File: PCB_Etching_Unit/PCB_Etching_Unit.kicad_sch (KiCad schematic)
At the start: 89 parts, among them M1 Motor_DC, M2 Motor_DC, Q1 TIP42, Q10 TIP42, Q11 TIP41, Q12 2N3904, Q13 TIP42, Q14 BC550, Q15 BC550, Q16 BC550, Q17 BC550, Q18 BC550, Q19 BC550, Q2 TIP42, Q20 BC550, Q3 TIP42, Q4 TIP42, Q5 TIP42, Q6 TIP41, Q7 TIP41, Q8 TIP42, Q9 TIP41, SW1 SW_MEC_5G, SW2 SW_MEC_5G, SW3 SW_MEC_5G, SW4 SW_MEC_5G, SW5 SW_MEC_5G, SW6 SW_MEC_5G, SW7 SW_MEC_5G, U1 HDSP-7801, U11 4511, U2 HDSP-7801, U3 HDSP-7801, U4 HDSP-7801, U5 4027, U6 4027, U9 4011

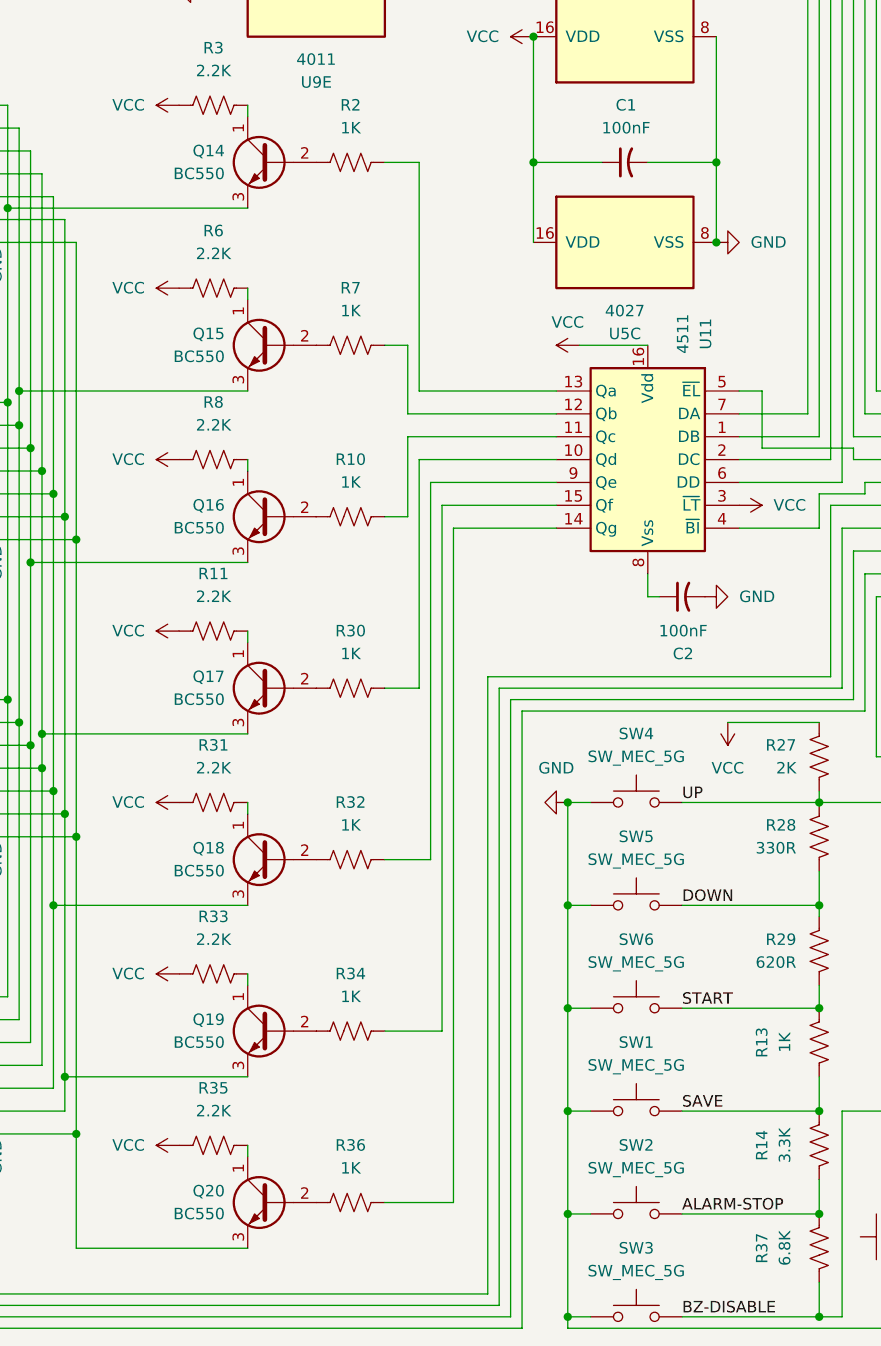
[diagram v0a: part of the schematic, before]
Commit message: 4511 pulls output low to activate, replaced NPN with PNP transistors to do that
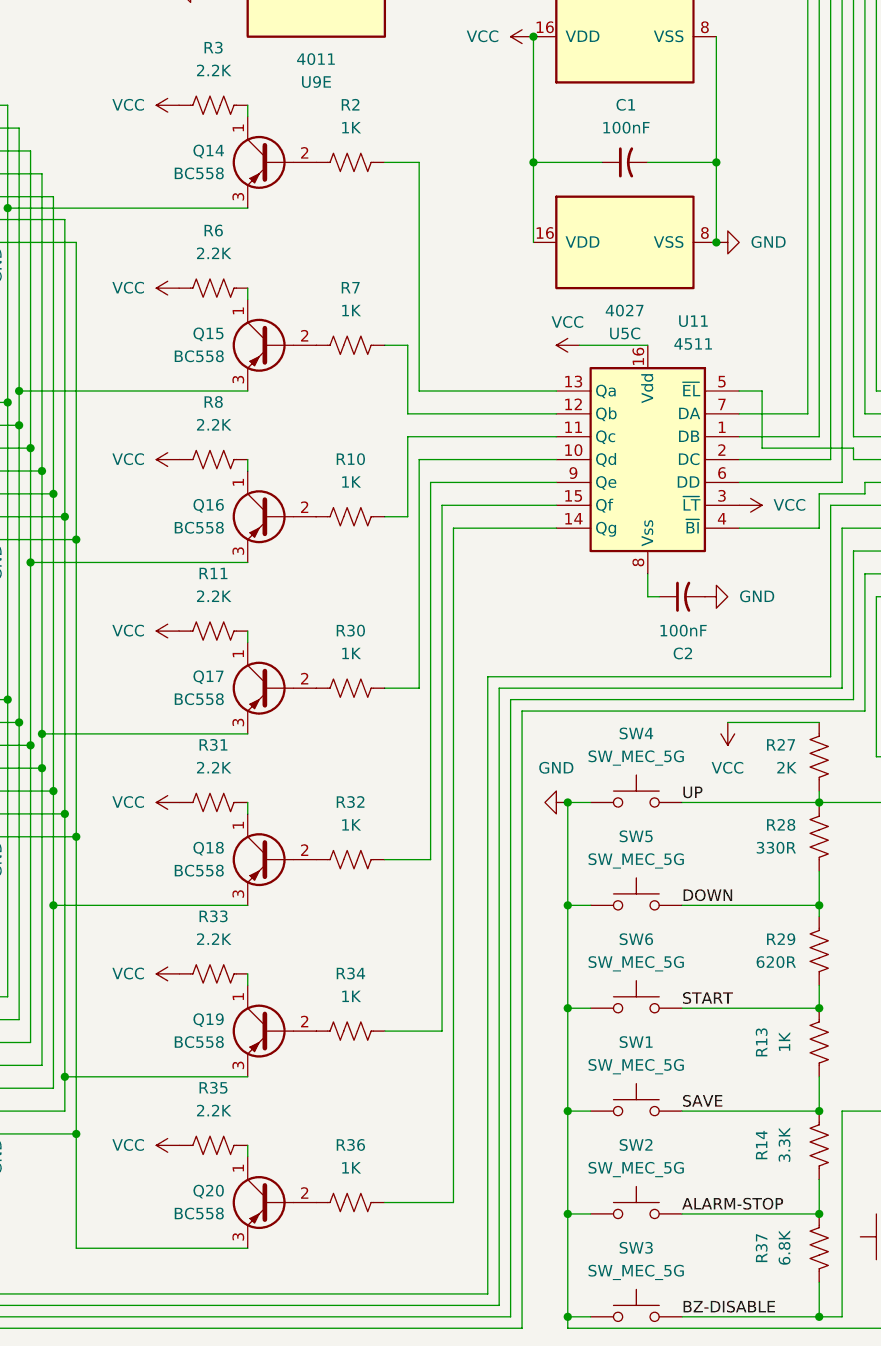
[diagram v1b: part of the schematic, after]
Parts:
- removed Q14, Q15, Q16, Q17, Q18, Q19, Q20: BC550, Package_TO_SOT_THT:TO-92_Inline, symbol Transistor_BJT:BC550
- added Q14, Q15, Q16, Q17, Q18, Q19, Q20: BC558, Package_TO_SOT_THT:TO-92_Inline, symbol Transistor_BJT:BC558
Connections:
- net at R6.2: now also Q15.1 (C)
- net at R31.2: now also Q18.1 (C)
- net at R32.1: now also Q18.2 (B)
- net at U1.4 (E), U2.4 (E), U3.4 (E)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: now also Q18.3 (E)
- net at R36.1: now also Q20.2 (B)
- net at R30.1: now also Q17.2 (B)
- net at R3.1: now also Q14.1 (C)
- net at R2.1: now also Q14.2 (B)
- net at U1.10 (A), U2.10 (A), U3.10 (A)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: now also Q14.3 (E)
- net at R35.2: now also Q20.1 (C)
- net at U1.3 (G), U2.3 (G), U3.3 (G)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: now also Q20.3 (E)
- net at R7.1: now also Q15.2 (B)
- net at U1.9 (B), U2.9 (B), U3.9 (B)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: now also Q15.3 (E)
- net at U1.2 (F), U2.2 (F), U3.2 (F)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: now also Q19.3 (E)
- net at U1.5 (D), U2.5 (D), U3.5 (D)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: now also Q17.3 (E)
- net at U1.8 (C), U2.8 (C), U3.8 (C)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: now also Q16.3 (E)
- net at R8.2: now also Q16.1 (C)
- net at R34.1: now also Q19.2 (B)
- net at R11.2: now also Q17.1 (C)
- net at R33.2: now also Q19.1 (C)
- net at R10.1: now also Q16.2 (B)

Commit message: Updated doc
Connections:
- net at R6.2: now also Q15.3 (E); no longer Q15.1 (C)
- net at Q18.1 (C): now also U1.4 (E), U2.4 (E), U3.4 (E), U4.4 (E); no longer R31.2
- net at Q20.1 (C): now also U1.3 (G), U2.3 (G), U3.3 (G), U4.3 (G); no longer R35.2
- net at U1.10 (A), U2.10 (A), U3.10 (A)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: now also Q14.1 (C); no longer Q14.3 (E)
- net at U1.2 (F), U2.2 (F), U3.2 (F)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: now also Q19.1 (C); no longer Q19.3 (E)
- net at U1.5 (D), U2.5 (D), U3.5 (D)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: now also Q17.1 (C); no longer Q17.3 (E)
- net at U1.8 (C), U2.8 (C), U3.8 (C)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: now also Q16.1 (C); no longer Q16.3 (E)
- net at U1.9 (B), U2.9 (B), U3.9 (B)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: now also Q15.1 (C); no longer Q15.3 (E)
- net at R3.1: now also Q14.3 (E); no longer Q14.1 (C)
- net at R8.2: now also Q16.3 (E); no longer Q16.1 (C)
- net at R11.2: now also Q17.3 (E); no longer Q17.1 (C)
- net at R33.2: now also Q19.3 (E); no longer Q19.1 (C)
- new net: Q18.3 (E), R31.2
- new net: Q20.3 (E), R35.2
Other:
- moved on the sheet: Q14, Q15, Q16, Q17, Q18, Q19, Q20
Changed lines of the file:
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@@
 	(wire
 		(pts
-			(xy 157.48 104.14) (xy 157.48 102.87)
+			(xy 156.21 104.14) (xy 156.21 102.87)
 		)
 		(stroke
@@
 	(wire
 		(pts
-			(xy 157.48 102.87) (xy 163.83 102.87)
+			(xy 156.21 102.87) (xy 163.83 102.87)
 		)
 		(stroke
@@
 	(wire
 		(pts
-			(xy 152.4 104.14) (xy 157.48 104.14)
+			(xy 152.4 104.14) (xy 156.21 104.14)
 		)
 		(stroke
@@
 	(symbol
 		(lib_id "Transistor_BJT:BC558")
-		(at 91.44 144.78 0)
-		(mirror y)
+		(at 91.44 144.78 180)
 		(unit 1)
 		(exclude_from_sim no)
@@
 		(on_board yes)
 		(dnp no)
-		(fields_autoplaced yes)
 		(property "Reference" "Q18"
-			(at 86.36 143.5099 0)
+			(at 86.36 146.0501 0)
 			(effects
 				(font
@@
 		)
 		(property "Value" "BC558"
-			(at 86.36 146.0499 0)
+			(at 86.36 143.5101 0)
 			(effects
 				(font
@@
 		)
 		(property "Footprint" "Package_TO_SOT_THT:TO-92_Inline"
-			(at 86.36 146.685 0)
+			(at 86.36 142.875 0)
 			(effects
 				(font
@@
 	(symbol
 		(lib_id "Transistor_BJT:BC558")
-		(at 91.44 182.88 0)
-		(mirror y)
+		(at 91.44 182.88 180)
 		(unit 1)
 		(exclude_from_sim no)
@@
 		(on_board yes)
 		(dnp no)
-		(fields_autoplaced yes)
 		(property "Reference" "Q20"
-			(at 86.36 181.6099 0)
+			(at 86.36 184.1501 0)
 			(effects
 				(font
@@
 		)
 		(property "Value" "BC558"
-			(at 86.36 184.1499 0)
+			(at 86.36 181.6101 0)
 			(effects
 				(font
@@
 		)
 		(property "Footprint" "Package_TO_SOT_THT:TO-92_Inline"
-			(at 86.36 184.785 0)
+			(at 86.36 180.975 0)
 			(effects
 				(font
@@
 	(symbol
 		(lib_id "Transistor_BJT:BC558")
-		(at 91.44 67.31 0)
-		(mirror y)
+		(at 91.44 67.31 180)
 		(unit 1)
 		(exclude_from_sim no)
@@
 		(on_board yes)
 		(dnp no)
-		(fields_autoplaced yes)
 		(property "Reference" "Q14"
-			(at 86.36 66.0399 0)
+			(at 86.36 68.5801 0)
 			(effects
 				(font
@@
 		)
 		(property "Value" "BC558"
-			(at 86.36 68.5799 0)
+			(at 86.36 66.0401 0)
 			(effects
 				(font
@@
 		)
 		(property "Footprint" "Package_TO_SOT_THT:TO-92_Inline"
-			(at 86.36 69.215 0)
+			(at 86.36 65.405 0)
 			(effects
 				(font
@@
 	(symbol
 		(lib_id "Transistor_BJT:BC558")
-		(at 91.44 87.63 0)
-		(mirror y)
+		(at 91.44 87.63 180)
 		(unit 1)
 		(exclude_from_sim no)
@@
 		(on_board yes)
 		(dnp no)
-		(fields_autoplaced yes)
 		(property "Reference" "Q15"
-			(at 86.36 86.3599 0)
+			(at 86.36 88.9001 0)
 			(effects
 				(font
@@
 		)
 		(property "Value" "BC558"
-			(at 86.36 88.8999 0)
+			(at 86.36 86.3601 0)
 			(effects
 				(font
@@
 		)
 		(property "Footprint" "Package_TO_SOT_THT:TO-92_Inline"
-			(at 86.36 89.535 0)
+			(at 86.36 85.725 0)
 			(effects
 				(font
@@
 	(symbol
 		(lib_id "Transistor_BJT:BC558")
-		(at 91.44 163.83 0)
-		(mirror y)
+		(at 91.44 163.83 180)
 		(unit 1)
 		(exclude_from_sim no)
@@
 		(on_board yes)
 		(dnp no)
-		(fields_autoplaced yes)
 		(property "Reference" "Q19"
-			(at 86.36 162.5599 0)
+			(at 86.36 165.1001 0)
 			(effects
 				(font
@@
 		)
 		(property "Value" "BC558"
-			(at 86.36 165.0999 0)
+			(at 86.36 162.5601 0)
 			(effects
 				(font
@@
 		)
 		(property "Footprint" "Package_TO_SOT_THT:TO-92_Inline"
-			(at 86.36 165.735 0)
+			(at 86.36 161.925 0)
 			(effects
 				(font
@@
 	(symbol
 		(lib_id "Transistor_BJT:BC558")
-		(at 91.44 125.73 0)
-		(mirror y)
+		(at 91.44 125.73 180)
 		(unit 1)
 		(exclude_from_sim no)
@@
 		(on_board yes)
 		(dnp no)
-		(fields_autoplaced yes)
 		(property "Reference" "Q17"
-			(at 86.36 124.4599 0)
+			(at 86.36 127.0001 0)
 			(effects
 				(font
@@
 		)
 		(property "Value" "BC558"
-			(at 86.36 126.9999 0)
+			(at 86.36 124.4601 0)
 			(effects
 				(font
@@
 		)
 		(property "Footprint" "Package_TO_SOT_THT:TO-92_Inline"
-			(at 86.36 127.635 0)
+			(at 86.36 123.825 0)
 			(effects
 				(font
@@
 	(symbol
 		(lib_id "Transistor_BJT:BC558")
-		(at 91.44 106.68 0)
-		(mirror y)
+		(at 91.44 106.68 180)
 		(unit 1)
 		(exclude_from_sim no)
@@
 		(on_board yes)
 		(dnp no)
-		(fields_autoplaced yes)
 		(property "Reference" "Q16"
-			(at 86.36 105.4099 0)
+			(at 86.36 107.9501 0)
 			(effects
 				(font
@@
 		)
 		(property "Value" "BC558"
-			(at 86.36 107.9499 0)
+			(at 86.36 105.4101 0)
 			(effects
 				(font
@@
 		)
 		(property "Footprint" "Package_TO_SOT_THT:TO-92_Inline"
-			(at 86.36 108.585 0)
+			(at 86.36 104.775 0)
 			(effects
 				(font

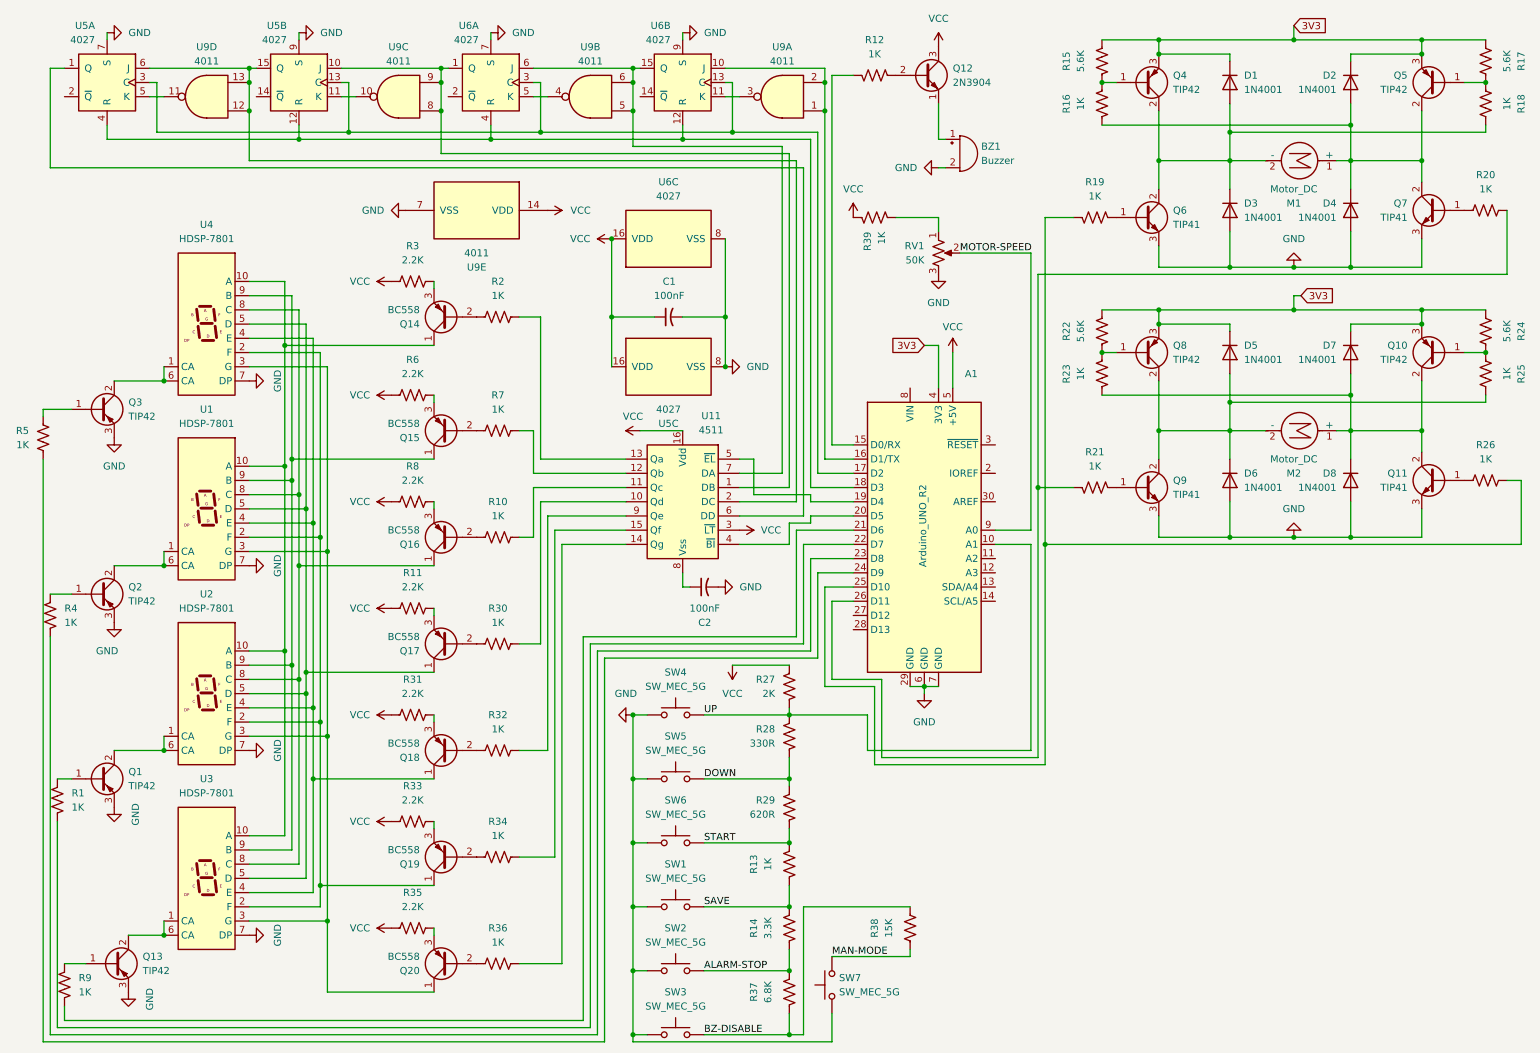
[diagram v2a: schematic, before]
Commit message: Next person to mix up PNP transistors gets bolted. Flipped transistors at segment output
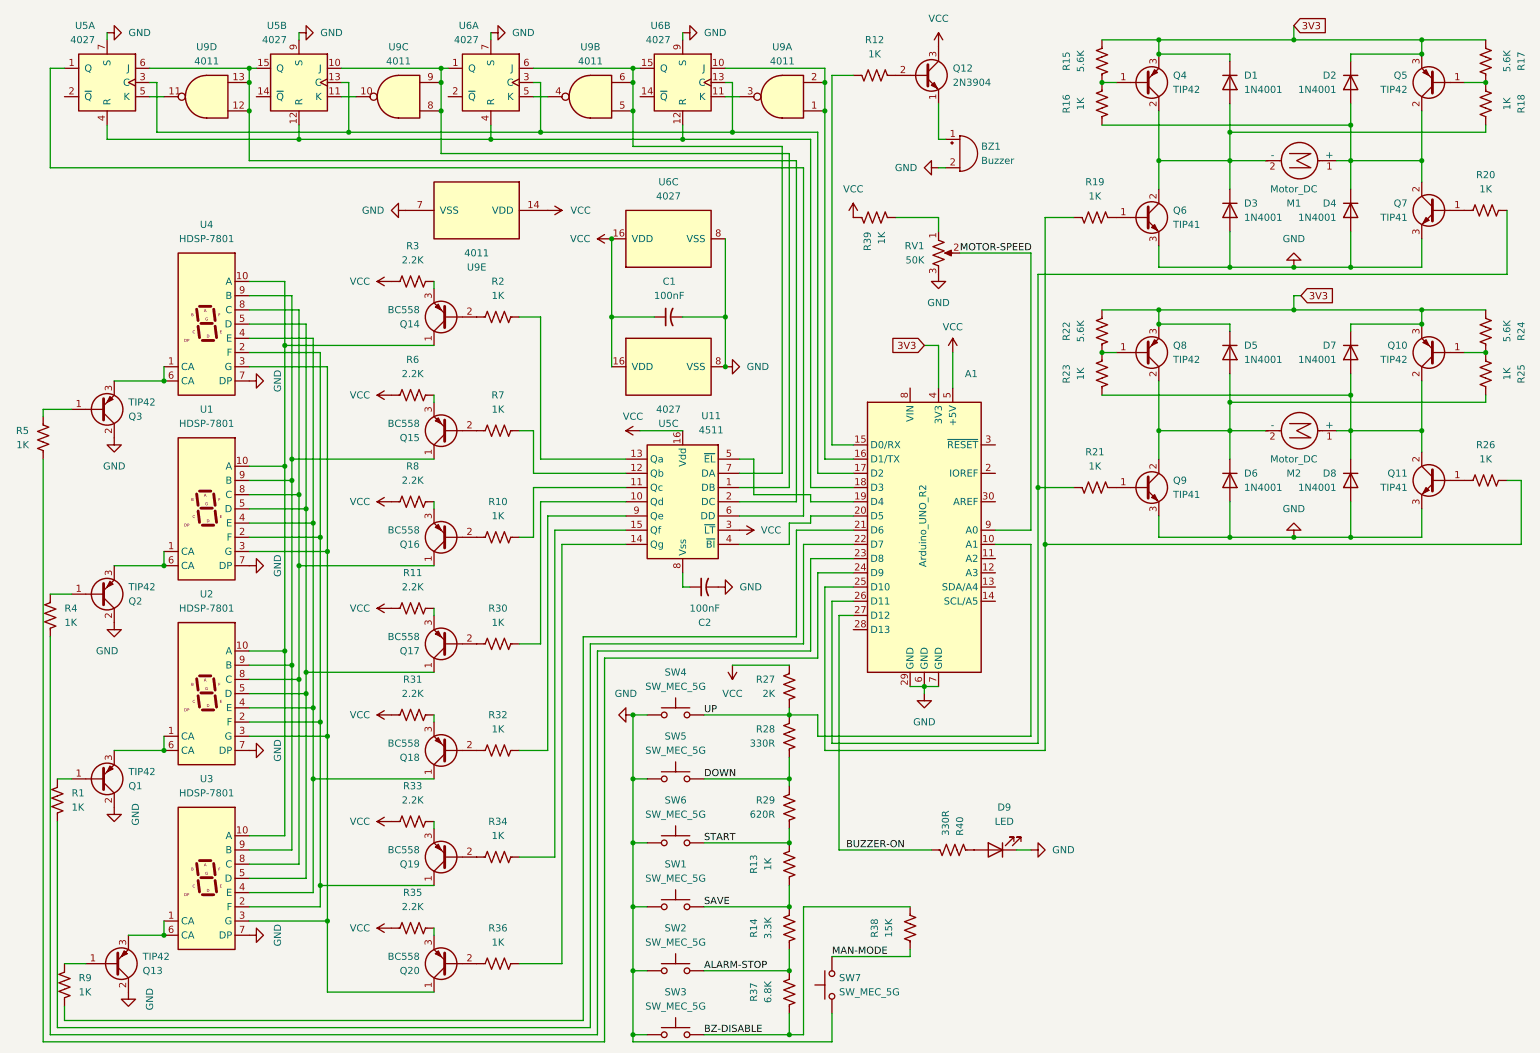
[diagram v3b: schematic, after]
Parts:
- added D9: LED, LED_THT:LED_D3.0mm, symbol Device:LED
- added R40: 330R, Resistor_THT:R_Axial_DIN0204_L3.6mm_D1.6mm_P7.62mm_Horizontal, symbol Device:R_US
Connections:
- net GND: now also Q1.2 (C), Q13.2 (C), Q2.2 (C), Q3.2 (C), D9.1 (K); no longer Q1.3 (E), Q13.3 (E), Q2.3 (E), Q3.3 (E)
- net at U3.1 (CA), U3.6 (CA): now also Q13.3 (E); no longer Q13.2 (C)
- net at U4.1 (CA), U4.6 (CA): now also Q3.3 (E); no longer Q3.2 (C)
- net at U1.1 (CA), U1.6 (CA): now also Q2.3 (E); no longer Q2.2 (C)
- net at U2.1 (CA), U2.6 (CA): now also Q1.3 (E); no longer Q1.2 (C)
- net BUZZER-ON: now reaches A1.27 (D12)
- net BUZZER-ON: now also R40.1
- new net: D9.2 (A), R40.2
